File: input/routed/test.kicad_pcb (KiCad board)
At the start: 2 copper layers, 54 x 34 mm, 11 parts, among them T1 Flactyl 4.0 (test), T2 x, T3 y

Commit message: All SMP works fine
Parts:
- removed T3: y, somelogo
- added D3: D_SOD-523, D_SOD-523, B.Cu at (0.00, -17.0)
- added D4: D_SOD-523, D_SOD-523, B.Cu at (0.00, 0.00)
- added D5: D_SOD-523, D_SOD-523, B.Cu at (86.4, -53.6)
- added D6: D_SOD-523, D_SOD-523, B.Cu at (86.4, -36.6)
- added JB2: JST_SH_SM02B-SRSS-TB_1x02-1MP_P1.00mm_Horizontal, JST_SH_SM02B-SRSS-TB_1x02-1MP_P1.00mm_Horizontal, B.Cu at (36.0, -34.0)
- added JB3: JST_SH_SM02B-SRSS-TB_1x02-1MP_P1.00mm_Horizontal, JST_SH_SM02B-SRSS-TB_1x02-1MP_P1.00mm_Horizontal, B.Cu at (36.0, -17.0)
- added JB4: JST_SH_SM02B-SRSS-TB_1x02-1MP_P1.00mm_Horizontal, JST_SH_SM02B-SRSS-TB_1x02-1MP_P1.00mm_Horizontal, B.Cu at (36.0, 0.00)
- added JC2: , JST_SH_SM05B-SRSS-TB_1x05-1MP_P1.00mm_Horizontal, B.Cu at (18.0, -34.0)
- added JC3: , JST_SH_SM05B-SRSS-TB_1x05-1MP_P1.00mm_Horizontal, B.Cu at (18.0, -17.0)
- added JC4: , JST_SH_SM05B-SRSS-TB_1x05-1MP_P1.00mm_Horizontal, B.Cu at (18.0, 0.00)
- added SB2: b3u-1000P, b3u-1000P, B.Cu at (54.0, -34.0)
- added SB3: b3u-1000P, b3u-1000P, B.Cu at (54.0, -17.0)
- added SB4: b3u-1000P, b3u-1000P, B.Cu at (54.0, 0.00)
- added SB5: b3u-1000P, b3u-1000P, B.Cu at (36.0, -51.0)
- added SS2: SW-TH_MSK12C02-HB-1, easyeda:SW-TH_MSK12C02-HB-1, F.Cu at (72.0, -34.0)
- added SS3: SW-TH_MSK12C02-HB-1, easyeda:SW-TH_MSK12C02-HB-1, F.Cu at (72.0, -17.0)
- added SS4: SW-TH_MSK12C02-HB-1, easyeda:SW-TH_MSK12C02-HB-1, F.Cu at (72.0, 0.00)
- SS1: value (none) -> SW-TH_MSK12C02-HB-1
- T1: value Flactyl 4.0 (test) -> x
- T2: value x -> y
- moved S1 96.2 mm to (90.0, -51.0)
- moved T2 80.7 mm to (0.00, -71.0)
- moved S2 74.0 mm to (90.0, -34.0)
- moved SS1 62.4 mm to (72.0, -51.0), turned to 0 degrees
- moved T1 61.6 mm to (60.0, -51.0), turned to 0 degrees
- moved JB1 54.1 mm to (36.0, -51.0), turned to 0 degrees
- moved JC1 54.1 mm to (18.0, -51.0), turned to 0 degrees
- moved SB1 38.5 mm to (54.0, -51.0)
- moved D1 36.8 mm to (0.00, -51.0), turned to 0 degrees
- moved D2 29.2 mm to (0.00, -34.0), turned to 90 degrees
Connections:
- D1 pad 1: R0 -> t
- D1 pad 2: C0R0D -> f
- D2 pad 1: R0 -> t
- D2 pad 2: C1R0D -> f
- S1 pad 1: C0R0D -> C5R0D
- S1 pad 2: C0 -> C5
- S1 pad 3: C0R0D -> C5R0D
- S1 pad 4: C0 -> C5
- S2 pad 1: C1R0D -> C5R1D
- S2 pad 2: C1 -> C5
- S2 pad 3: C1R0D -> C5R1D
- S2 pad 4: C1 -> C5
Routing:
- net R0: track 31.4 -> 0.00 mm
- net GND: track 22.0 -> 0.00 mm
- net BSLI: track 17.9 -> 0.00 mm
- net RST: track 0.00 -> 16.0 mm
- net C0R0D: track 13.0 -> 0.00 mm
- net C1R0D: track 3.77 -> 0.00 mm
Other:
- board size 54 x 34 mm -> 108 x 68 mm

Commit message: fix top slider
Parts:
- removed SB5: b3u-1000P, b3u-1000P
- SS1, SS2, SS3, SS4: value SW-TH_MSK12C02-HB-1 -> SW-SMD_JS202011JCQN; footprint easyeda:SW-TH_MSK12C02-HB-1 -> easyeda:SW-SMD_JS202011JCQN

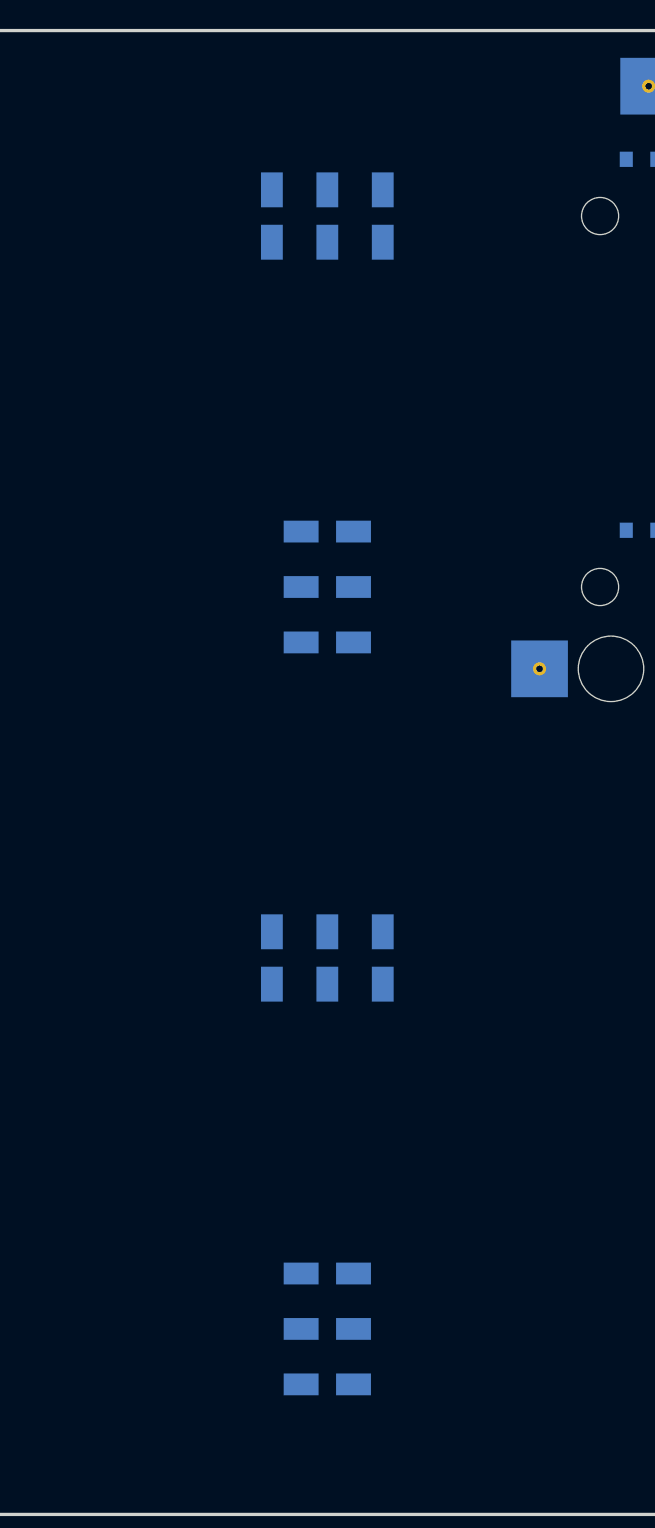
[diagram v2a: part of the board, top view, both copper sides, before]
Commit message: Fix top slider bom
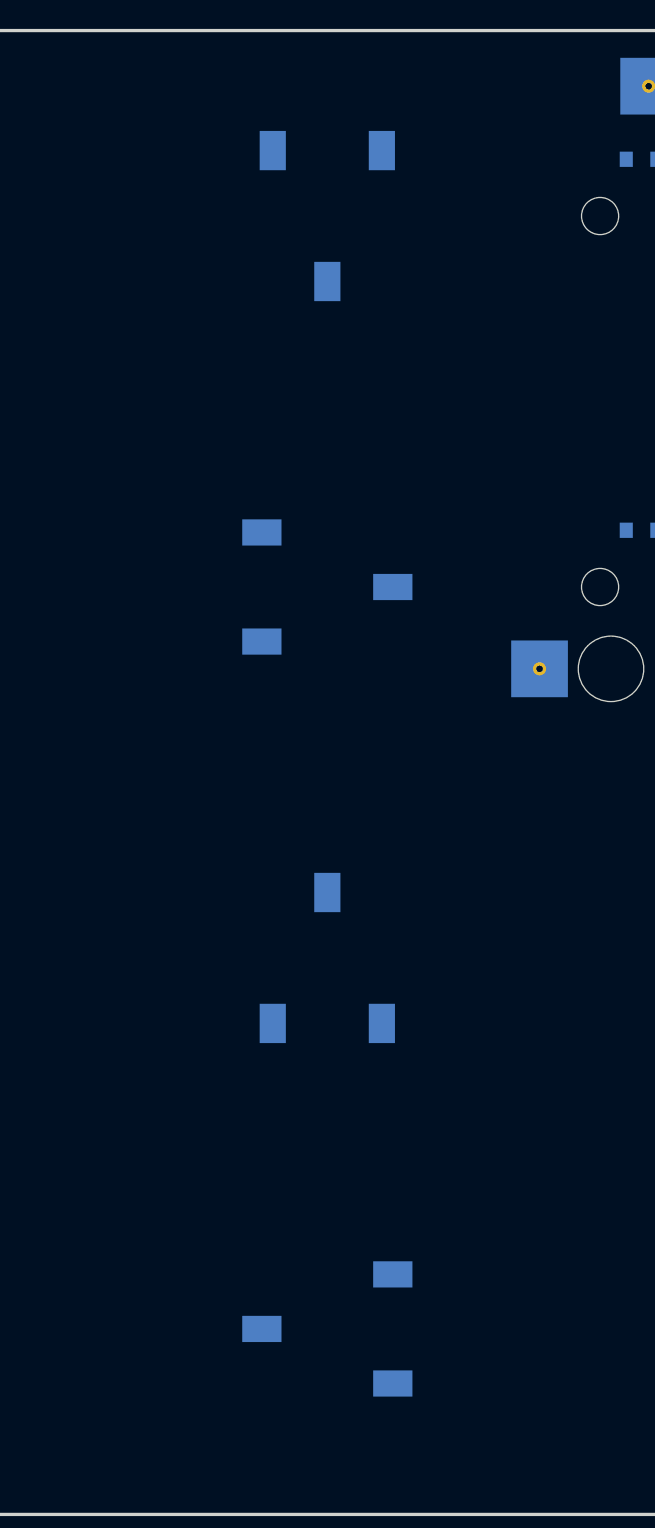
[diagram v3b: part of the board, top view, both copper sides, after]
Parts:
- SS1, SS2, SS3, SS4: value SW-SMD_JS202011JCQN -> SW-SMD_SS-3235D-03-L2.00; footprint easyeda:SW-SMD_JS202011JCQN -> easyeda:SW-SMD_SS-3235D-03-L2.00; moved to B.Cu
